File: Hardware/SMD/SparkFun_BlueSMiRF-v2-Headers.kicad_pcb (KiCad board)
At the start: 2 copper layers, 38.1 x 15.2 mm, 57 parts, among them J1 Conn_01x06, Q1 NMOS_0.2A_50V, Q2 NMOS_0.2A_50V, SW1 SPST_Momentary_4.6x2.8mm, U1 ESP32-PICO-V3-02, U2 AP2112K-3.3

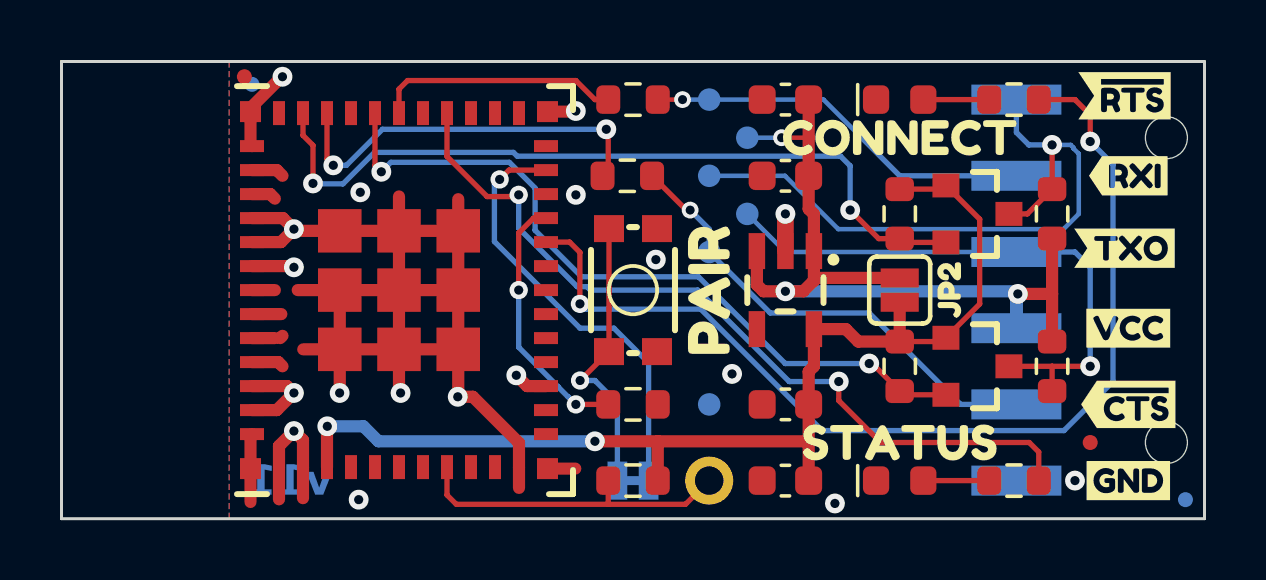
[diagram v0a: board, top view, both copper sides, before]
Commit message: Add 3D models
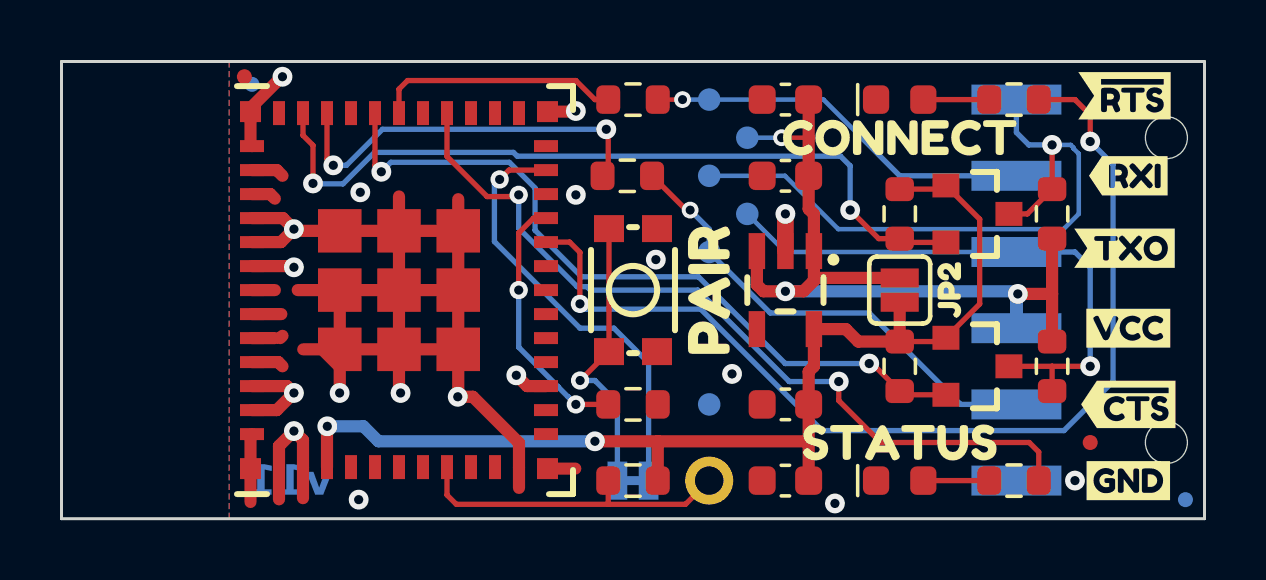
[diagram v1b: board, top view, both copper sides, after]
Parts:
- D1: footprint SparkFun-LED:LED_0603_1608Metric -> SparkFun-LED:LED_0603_1608Metric_Green
- D2: footprint SparkFun-LED:LED_0603_1608Metric -> SparkFun-LED:LED_0603_1608Metric_Red
- J1: footprint SparkFun-Connector:1X06-SMD_RA_MALE -> SparkFun-Connector:1x06_SMD_RA_Male
- JP1: footprint SparkFun-Jumper:SMT-JUMPER_2_NC_TRACE_SILK -> SparkFun-Jumper:Jumper_2_NC_Trace
- JP2: footprint SparkFun-Jumper:SMT-JUMPER_2_NO_SILK -> SparkFun-Jumper:Jumper_2_NO
- SW1: footprint SparkFun-Switch:Momentary_SMD_4.6x2.8mm -> SparkFun-Switch:Push_SMD_4.6x2.8mm_h2.5mm
- TP1: footprint SparkFun-Connector:1X01 -> SparkFun-Connector:1x01
- U1: footprint SparkFun-RF:ESP32-MINI -> SparkFun-RF:ESP32-PICO-MINI
- U3: footprint SparkFun-Aesthetic:ORDERING_INSTRUCTIONS -> SparkFun-Aesthetic:Ordering_Instructions
- turned R10 to -90 degrees
- turned R2 to 180 degrees
- turned R7 to 90 degrees
- turned R8 to 90 degrees
- turned R9 to 90 degrees
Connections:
- C3 pad 1: +3.3V -> 3.3V
- C4 pad 1: +3.3V -> 3.3V
- JP2 pad 2: +3.3V -> 3.3V
- Q1 pad 1: +3.3V -> 3.3V
- Q2 pad 1: +3.3V -> 3.3V
- R1 pad 1: +3.3V -> 3.3V
- R10 pad 1: VCC -> ~{RTS_HV}
- R10 pad 2: ~{RTS_HV} -> VCC
- R2 pad 1: Net-(U1-IOA15) -> GND
- R2 pad 2: GND -> Net-(U1-IOA15)
- R7 pad 1: +3.3V -> TX_LV
- R7 pad 2: TX_LV -> 3.3V
- R8 pad 1: +3.3V -> ~{RTS_LV}
- R8 pad 2: ~{RTS_LV} -> 3.3V
- R9 pad 1: VCC -> TX_HV
- R9 pad 2: TX_HV -> VCC
- U1 pad 3: +3.3V -> 3.3V
- U2 pad 5: +3.3V -> 3.3V
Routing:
- net 3.3V: track 0.00 -> 37.6 mm, vias 0 -> 2
- net +3.3V: track 37.6 -> 0.00 mm, vias 2 -> 0

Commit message: Update 3D models and components to current library
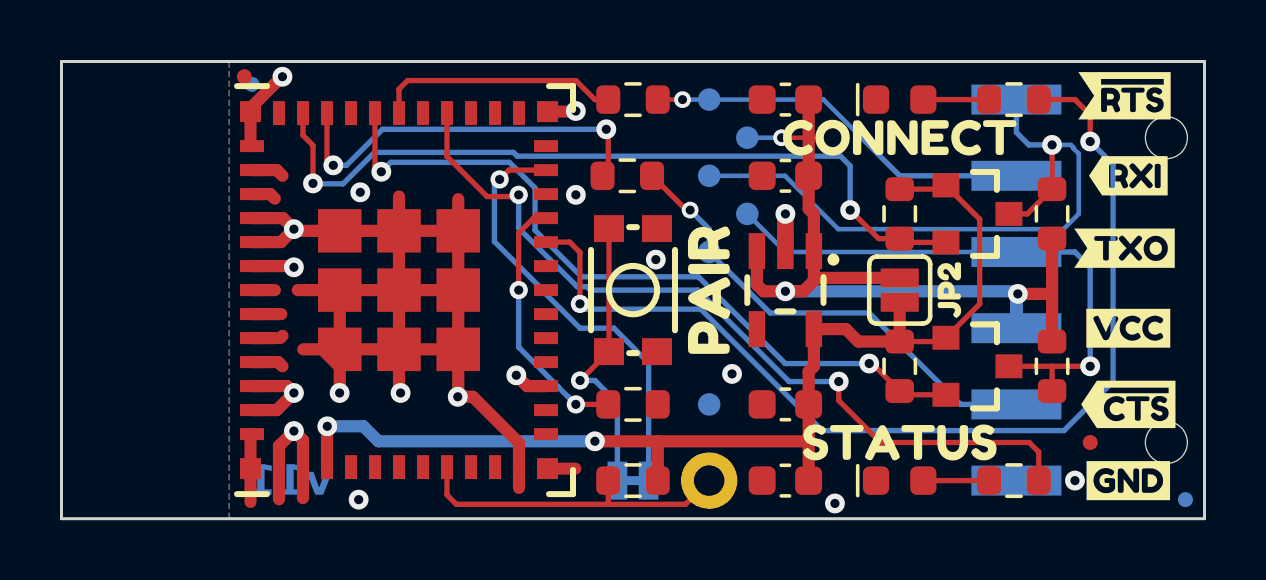
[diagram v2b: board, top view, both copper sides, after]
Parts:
- FID1, FID2, FID3, FID4: value Fiducial_0.5 -> Fiducial_0.5mm
- Q1, Q2: value NMOS_0.2A_50V -> BSS138
- SW1: value SPST_Momentary_4.6x2.8mm -> SMD_4.6x2.8mm_h2.5mm
- TP1: value TestPoint -> PTH
- TP2, TP3, TP4, TP5, TP6, TP7: value TestPoint_0.75mm -> 0.75mm
